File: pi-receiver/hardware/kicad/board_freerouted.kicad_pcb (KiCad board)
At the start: 2 copper layers, 65 x 56 mm, 40 parts, among them J1 RJ45_Amphenol_54602-x08_Horiz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, J2 PinSocket_2x20_P2.54mm_Vertic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, U1 MCP4922-E/SL, U2 MCP4922-E/SL, U3 MCP4922-E/SL, U4 MCP6004-I/ST, U5 MCP6004-I/ST

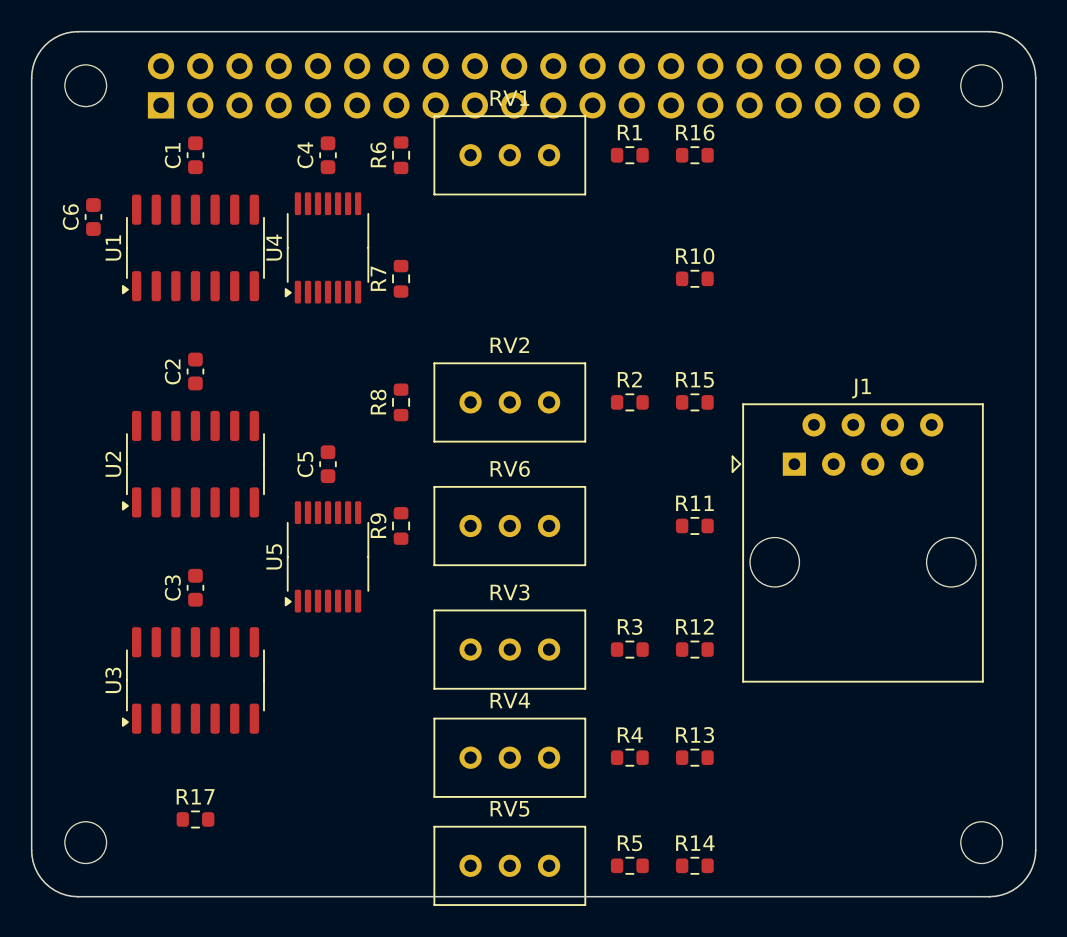
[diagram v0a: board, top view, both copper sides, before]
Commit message: Route the Pi laser HAT with Freerouting; export gerbers/BOM/CPL
Replaces the naive hand-written Manhattan router (417 DRC violations,
discarded - board_routed.kicad_pcb/route_board.py removed) with a real
autorouter via the standard KiCad<->Freerouting DSN/SES workflow:

- export_dsn.py: board.kicad_pcb (DRC-clean placement, unchanged) ->
  Specctra DSN, widening default trace width/clearance from KiCad's
  0.2mm to 0.25mm (DESIGN.md already called for generous clearance -
  this board has the room, no reason to push fab tolerances).
- Freerouting 2.4.1 run headless in Docker (needed a Java 25 JRE - the
  release jar's class file version is too new for Java 21/23). Fanout
  + 6 routing passes in ~7 seconds: 0 unrouted, 0 violations, score
  999.99/1000.
- import_ses.py: routed session imported back onto the board, saved as
  board_freerouted.kicad_pcb.

Final DRC: 0 errors, 7 warnings (cosmetic silkscreen-text clipping
only - doesn't affect fabrication). Also tightened up two mounting-hole
reference labels that were poking past the board edge.

With DRC actually clean, exported real fabrication output to
pi-receiver/hardware/gerbers/: Gerbers + drill (zipped), CPL, and a BOM
built from DESIGN.md's part table (JLCPCB numbers where known). Not
exported earlier because doing so from a non-clean board would have
misrepresented it as order-ready.

Freerouting's jar (64MB) isn't committed - re-download release v2.4.1
from GitHub to reproduce; see kicad/README.md for the exact commands.

Still outstanding before ordering: the RJ45 footprint is a generic
library stand-in for the actual BOM part (EVERCOM 5301-8P8C), not
verified against that part's own datasheet dimensions - see both
README.md files under hardware/ for the full honest status.

Co-Authored-By: Claude Sonnet 5 <noreply@anthropic.com>
Claude-Session: https://claude.ai/code/session_01X7ckCumaWad6JysqEZqZ4L
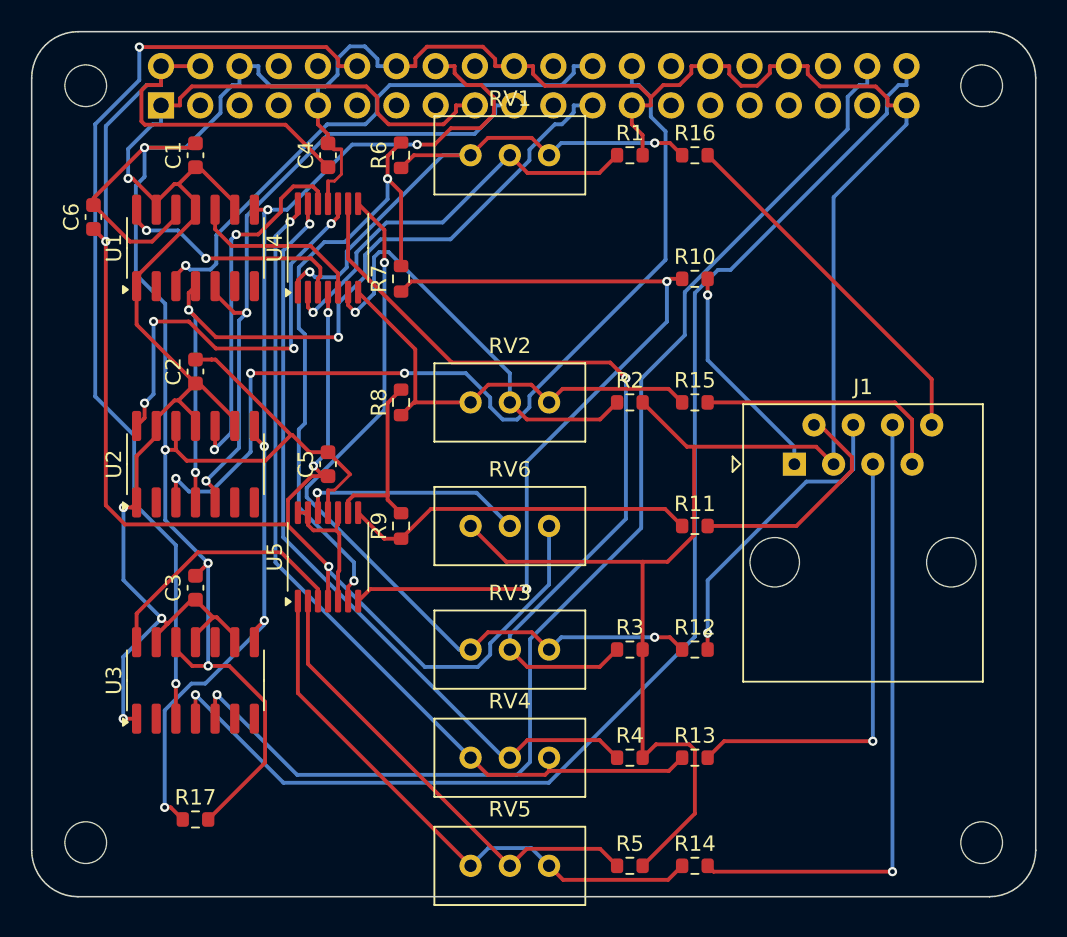
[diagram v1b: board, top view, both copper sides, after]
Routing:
- net GND: track 0.00 -> 260.9 mm, vias 0 -> 4
- net VDD_5V: track 0.00 -> 111.7 mm, vias 0 -> 4
- net VDD_3V3: track 0.00 -> 99.8 mm, vias 0 -> 4
- net SPI1_SCK: track 0.00 -> 83.5 mm, vias 0 -> 1
- net SPI1_SDI: track 0.00 -> 78.7 mm, vias 0 -> 1
- net LDAC: track 0.00 -> 70.8 mm, vias 0 -> 5
- net SPI1_CE0: track 0.00 -> 61.7 mm, vias 0 -> 2
- net SPI0_CE1: track 0.00 -> 59.8 mm, vias 0 -> 3
- net SIG_G: track 0.00 -> 57.2 mm, vias 0 -> 1
- net X_MINUS: track 0.00 -> 53.4 mm, vias 0 -> 2
- net R_FB: track 0.00 -> 53.3 mm, vias 0 -> 1
- net SIG_R: track 0.00 -> 51.8 mm, vias 0 -> 2
- net G_FB: track 0.00 -> 50.8 mm, vias 0 -> 1
- net SPI0_SCK: track 0.00 -> 50.3 mm, vias 0 -> 3
- net SPI0_SDI: track 0.00 -> 43.5 mm, vias 0 -> 2
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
